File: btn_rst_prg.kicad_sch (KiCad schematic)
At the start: 8 parts

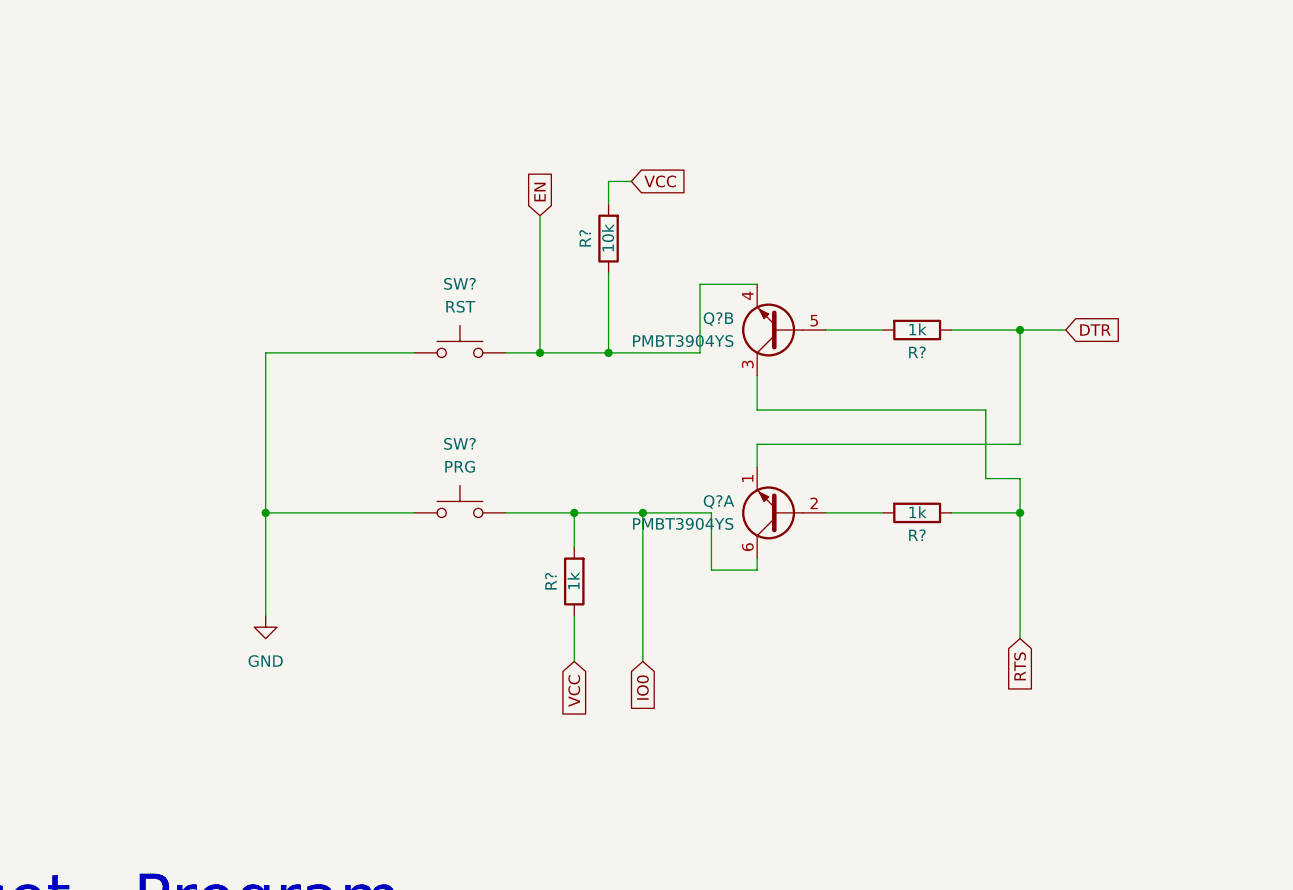
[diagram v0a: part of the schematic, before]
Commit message: add salidas separadas 1,2,3
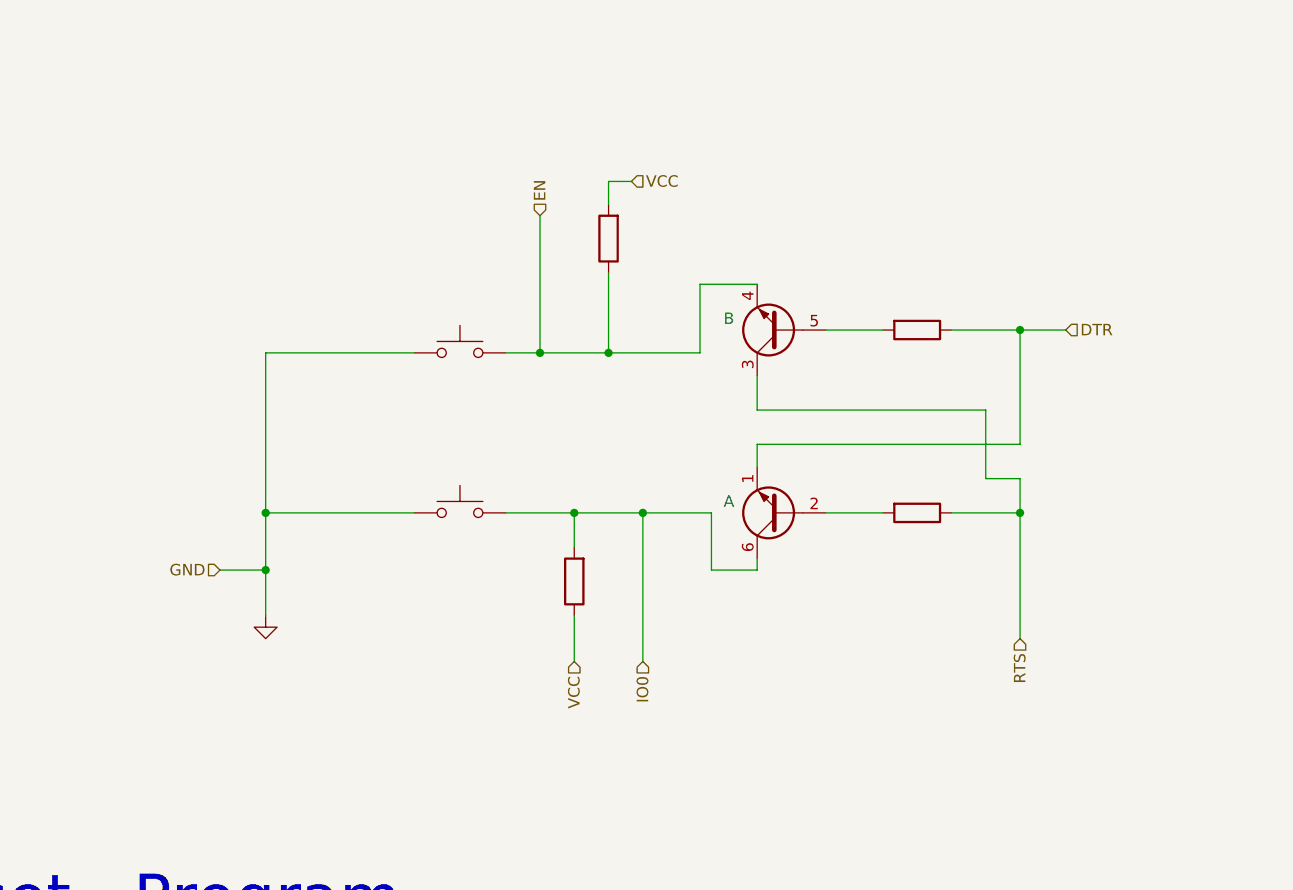
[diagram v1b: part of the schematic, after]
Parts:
- ?: renamed from SW?; value RST -> (none); footprint Button_Switch_SMD:SW_SPST_CK_RS282G05A3 -> (none)
- ?: renamed from SW?; value PRG -> (none); footprint Button_Switch_SMD:SW_SPST_CK_RS282G05A3 -> (none)
- ?: renamed from R?; value 10k -> (none); footprint Resistor_SMD:R_0603_1608Metric_Pad0.98x0.95mm_HandSolder -> (none)
- ? (x2): renamed from Q?; value PMBT3904YS -> (none); footprint Package_TO_SOT_SMD:SOT-363_SC-70-6 -> (none)
- ? (x3): renamed from R?; value 1k -> (none); footprint Resistor_SMD:R_0603_1608Metric_Pad0.98x0.95mm_HandSolder -> (none)
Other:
- company: (none) -> INTEAMBI

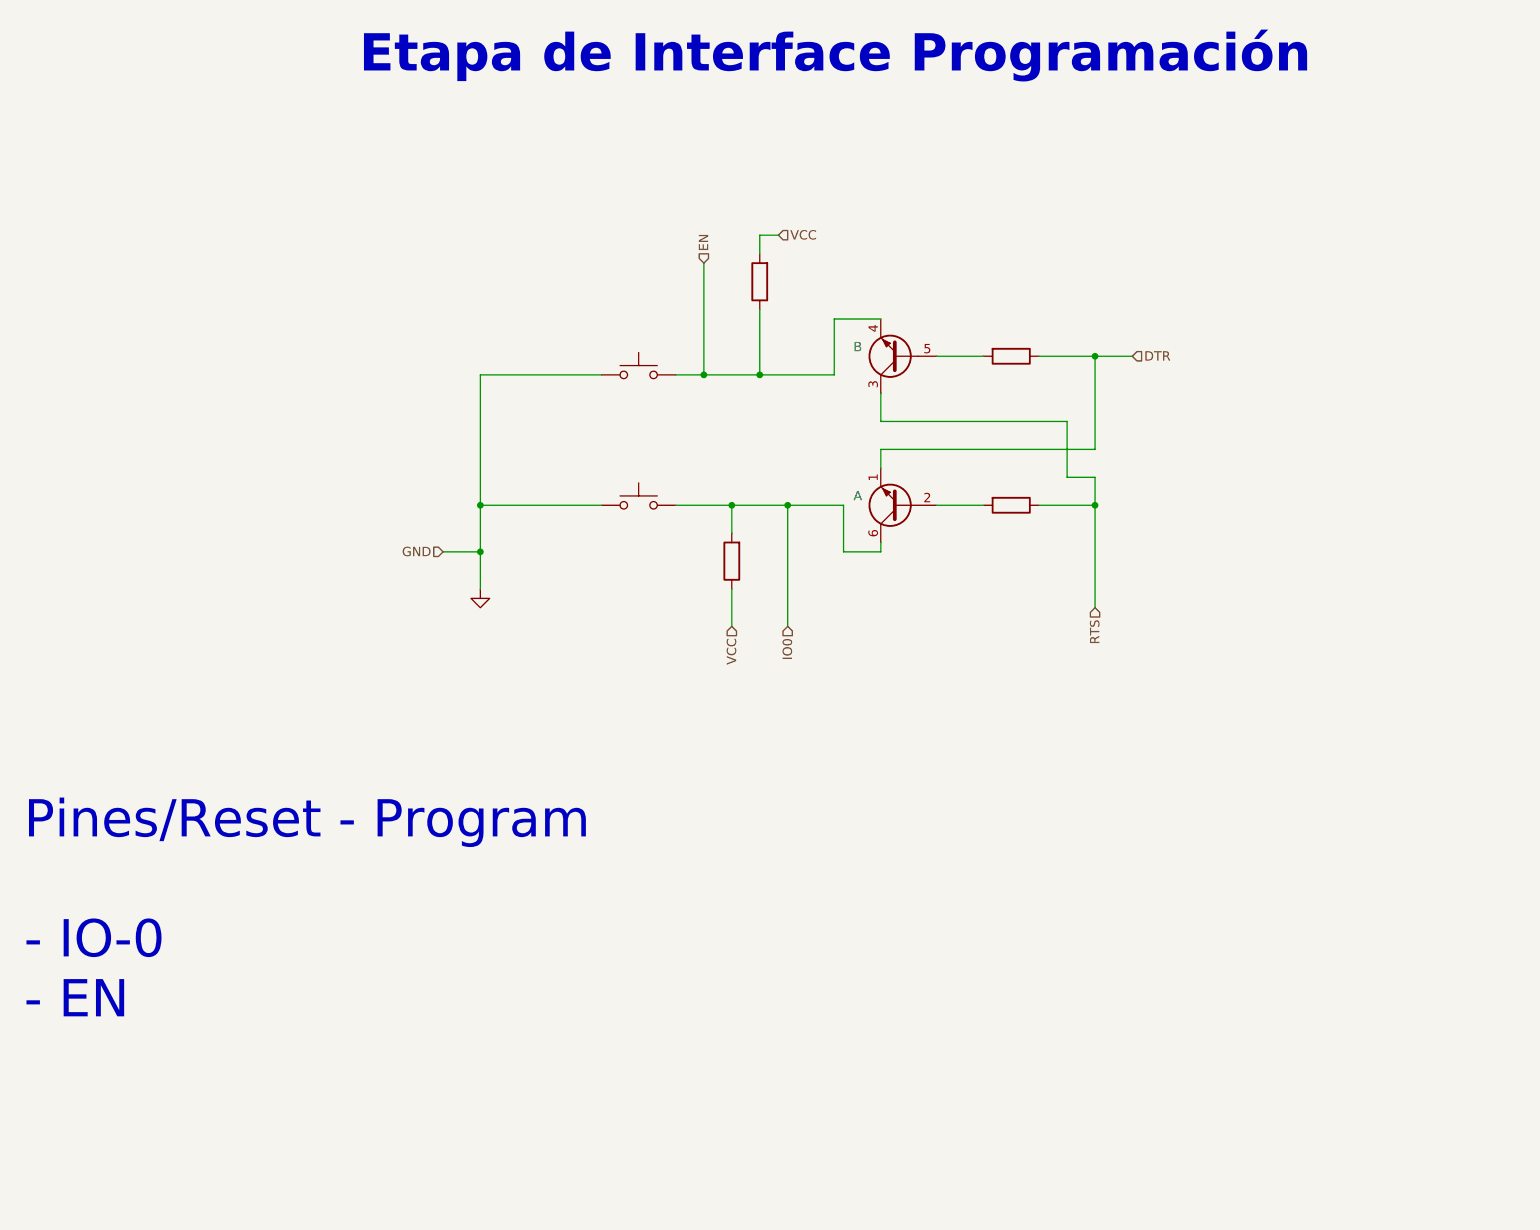
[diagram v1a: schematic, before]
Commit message: add entradas separadas
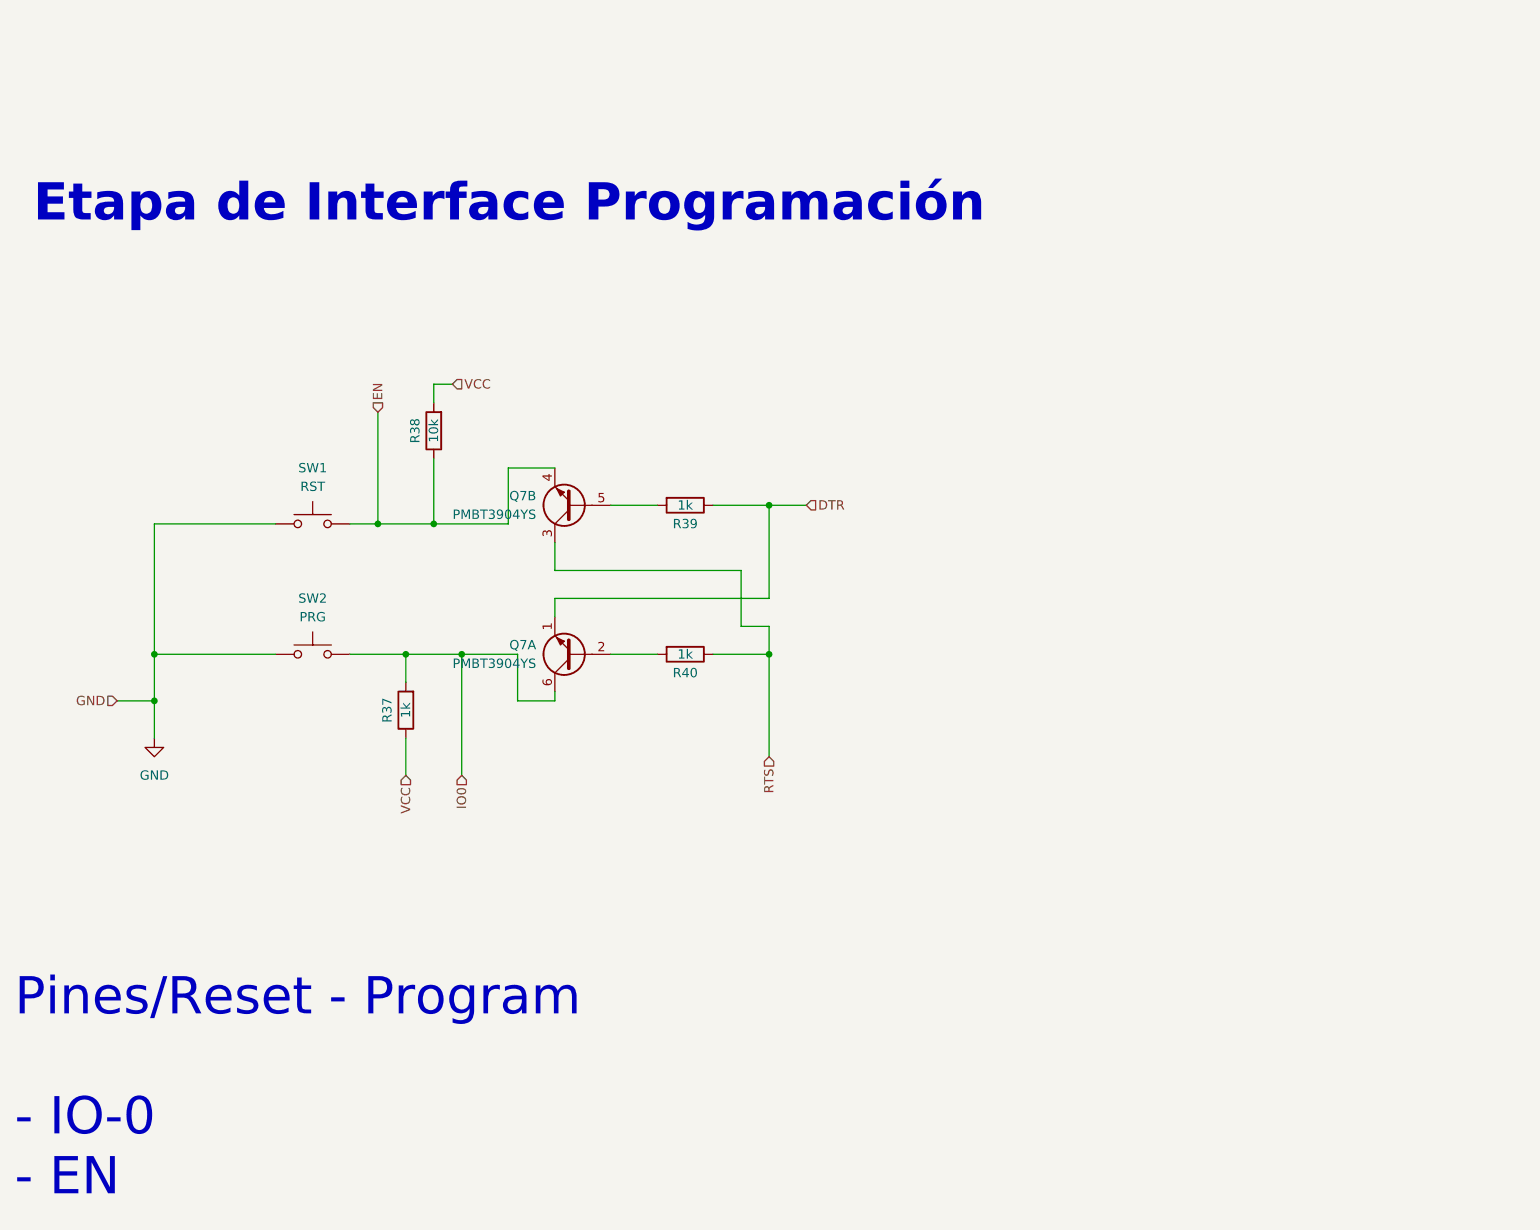
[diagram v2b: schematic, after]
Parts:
- Q7: renamed from ?; value (none) -> PMBT3904YS; footprint (none) -> Package_TO_SOT_SMD:SOT-363_SC-70-6
- R37, R40: renamed from ?; value (none) -> 1k; footprint (none) -> Resistor_SMD:R_0603_1608Metric
- R38: renamed from ?; value (none) -> 10k; footprint (none) -> Resistor_SMD:R_0603_1608Metric
- R39: renamed from ?; value (none) -> 1k; footprint (none) -> Resistor_SMD:R_0603_1608Metric_Pad0.98x0.95mm_HandSolder
- SW1: renamed from ?; value (none) -> RST; footprint (none) -> Button_Switch_SMD:SW_SPST_CK_RS282G05A3
- SW2: renamed from ?; value (none) -> PRG; footprint (none) -> Button_Switch_SMD:SW_SPST_CK_RS282G05A3
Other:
- moved on the sheet: Q7A, Q7B

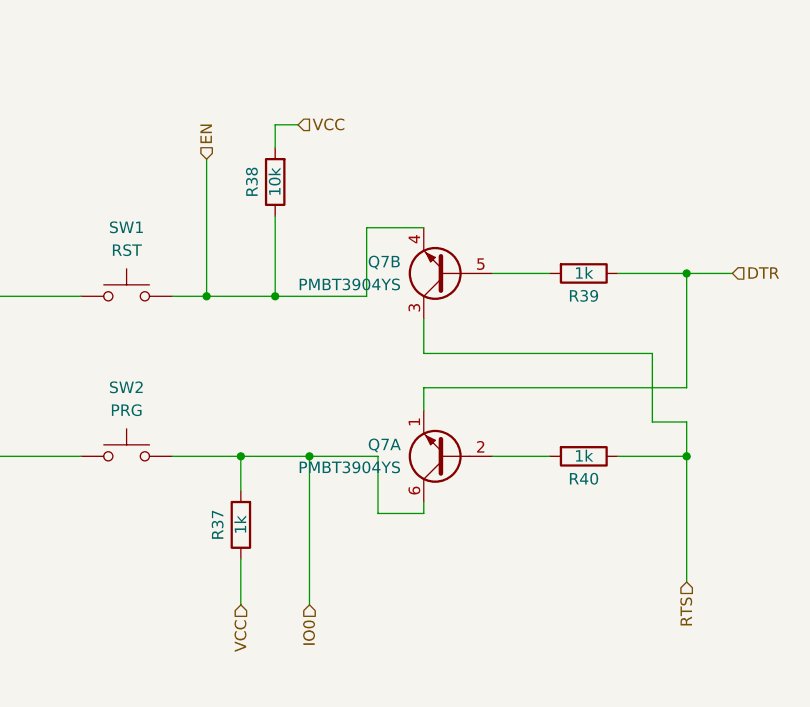
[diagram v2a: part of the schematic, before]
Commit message: input/output separadas
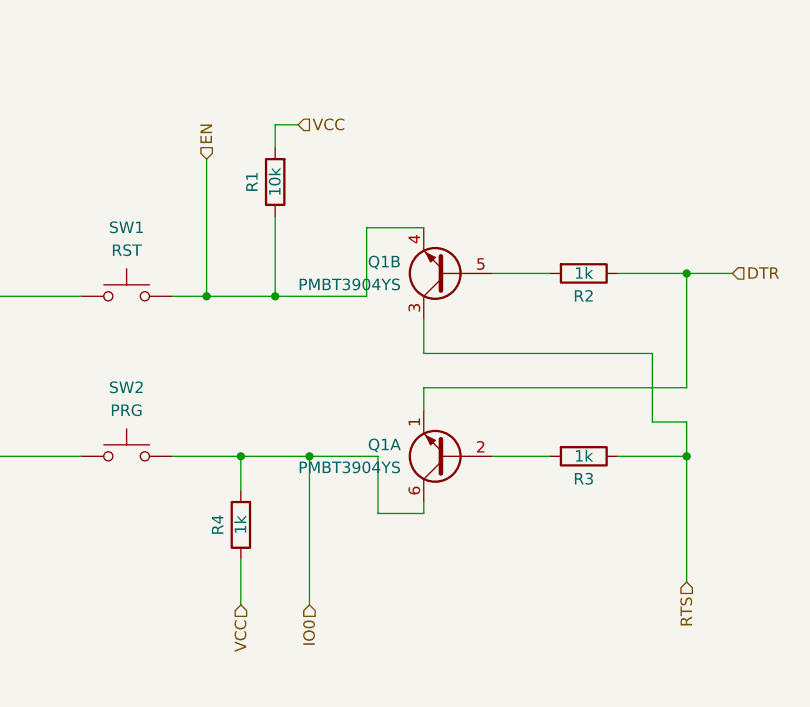
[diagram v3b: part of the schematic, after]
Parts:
- renumbered Q7 to Q1, R38 to R1, R39 to R2, R40 to R3, R37 to R4
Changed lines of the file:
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@@
   (paper "A4" portrait)
   (title_block
-    (date "2022-09-15")
+    (date "2022-10-09")
     (rev "José Luis Laica")
     (company "INTEAMBI")
@@
   (symbol (lib_id "Device:R") (at 93.98 93.98 180) (unit 1)
     (in_bom yes) (on_board yes) (dnp no)
-    (property "Reference" "R38" (at 91.44 93.98 90)
+    (property "Reference" "R1" (at 91.44 93.98 90)
       (effects (font (size 1.27 1.27)))
     )
@@
       (project "PLC 32 V2"
         (path "/d17a54f1-6eda-453f-95e1-42a53b02a1c3/42521a84-9a19-4c46-b1f2-db09ca0e83df"
-          (reference "R38") (unit 1) (value "10k") (footprint "Resistor_SMD:R_0603_1608Metric")
+          (reference "R1") (unit 1) (value "10k") (footprint "Resistor_SMD:R_0603_1608Metric")
         )
       )
@@
   (symbol (lib_id "Transistor_BJT:PMBT3904YS") (at 113.03 124.46 180) (unit 1)
     (in_bom yes) (on_board yes) (dnp no) (fields_autoplaced)
-    (property "Reference" "Q7" (at 107.95 123.1899 0)
+    (property "Reference" "Q1" (at 107.95 123.1899 0)
       (effects (font (size 1.27 1.27)) (justify left))
     )
@@
       (project "PLC 32 V2"
         (path "/d17a54f1-6eda-453f-95e1-42a53b02a1c3/42521a84-9a19-4c46-b1f2-db09ca0e83df"
-          (reference "Q7") (unit 1) (value "PMBT3904YS") (footprint "Package_TO_SOT_SMD:SOT-363_SC-70-6")
+          (reference "Q1") (unit 1) (value "PMBT3904YS") (footprint "Package_TO_SOT_SMD:SOT-363_SC-70-6")
         )
       )
@@
   (symbol (lib_id "Device:R") (at 128.27 104.14 270) (unit 1)
     (in_bom yes) (on_board yes) (dnp no)
-    (property "Reference" "R39" (at 128.27 106.68 90)
+    (property "Reference" "R2" (at 128.27 106.68 90)
       (effects (font (size 1.27 1.27)))
     )
@@
       (project "PLC 32 V2"
         (path "/d17a54f1-6eda-453f-95e1-42a53b02a1c3/42521a84-9a19-4c46-b1f2-db09ca0e83df"
-          (reference "R39") (unit 1) (value "1k") (footprint "Resistor_SMD:R_0603_1608Metric_Pad0.98x0.95mm_HandSolder")
+          (reference "R2") (unit 1) (value "1k") (footprint "Resistor_SMD:R_0603_1608Metric_Pad0.98x0.95mm_HandSolder")
         )
       )
@@
   (symbol (lib_id "Transistor_BJT:PMBT3904YS") (at 113.03 104.14 180) (unit 2)
     (in_bom yes) (on_board yes) (dnp no) (fields_autoplaced)
-    (property "Reference" "Q7" (at 107.95 102.8699 0)
+    (property "Reference" "Q1" (at 107.95 102.8699 0)
       (effects (font (size 1.27 1.27)) (justify left))
     )
@@
       (project "PLC 32 V2"
         (path "/d17a54f1-6eda-453f-95e1-42a53b02a1c3/42521a84-9a19-4c46-b1f2-db09ca0e83df"
-          (reference "Q7") (unit 2) (value "PMBT3904YS") (footprint "Package_TO_SOT_SMD:SOT-363_SC-70-6")
+          (reference "Q1") (unit 2) (value "PMBT3904YS") (footprint "Package_TO_SOT_SMD:SOT-363_SC-70-6")
         )
       )
@@
   (symbol (lib_id "power:GND") (at 55.88 135.89 0) (unit 1)
     (in_bom yes) (on_board yes) (dnp no) (fields_autoplaced)
-    (property "Reference" "#PWR028" (at 55.88 142.24 0)
+    (property "Reference" "#PWR03" (at 55.88 142.24 0)
       (effects (font (size 1.27 1.27)) hide)
     )
@@
       (project "PLC 32 V2"
         (path "/d17a54f1-6eda-453f-95e1-42a53b02a1c3/42521a84-9a19-4c46-b1f2-db09ca0e83df"
-          (reference "#PWR028") (unit 1) (value "GND") (footprint "")
+          (reference "#PWR03") (unit 1) (value "GND") (footprint "")
         )
       )
@@
   (symbol (lib_id "Device:R") (at 128.27 124.46 270) (unit 1)
     (in_bom yes) (on_board yes) (dnp no)
-    (property "Reference" "R40" (at 128.27 127 90)
+    (property "Reference" "R3" (at 128.27 127 90)
       (effects (font (size 1.27 1.27)))
     )
@@
       (project "PLC 32 V2"
         (path "/d17a54f1-6eda-453f-95e1-42a53b02a1c3/42521a84-9a19-4c46-b1f2-db09ca0e83df"
-          (reference "R40") (unit 1) (value "1k") (footprint "Resistor_SMD:R_0603_1608Metric")
+          (reference "R3") (unit 1) (value "1k") (footprint "Resistor_SMD:R_0603_1608Metric")
         )
       )
@@
   (symbol (lib_id "Device:R") (at 90.17 132.08 180) (unit 1)
     (in_bom yes) (on_board yes) (dnp no)
-    (property "Reference" "R37" (at 87.63 132.08 90)
+    (property "Reference" "R4" (at 87.63 132.08 90)
       (effects (font (size 1.27 1.27)))
     )
@@
       (project "PLC 32 V2"
         (path "/d17a54f1-6eda-453f-95e1-42a53b02a1c3/42521a84-9a19-4c46-b1f2-db09ca0e83df"
-          (reference "R37") (unit 1) (value "1k") (footprint "Resistor_SMD:R_0603_1608Metric")
-        )
-      )
+          (reference "R4") (unit 1) (value "1k") (footprint "Resistor_SMD:R_0603_1608Metric")
+        )
+      )
